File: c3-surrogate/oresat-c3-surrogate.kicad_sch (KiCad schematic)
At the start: 73 parts, among them J1 J-SAMTEC-TFM-120-X1-XXX-D-RA, J2 Conn_01x04, J4 Conn_01x02_Socket, Q1 PMV45EN, Q3 NTR4101P, Q4 NTR4101P, Q5 DMP3050LVT-7, SW2 EG1218, SW3 OS203011MV9QS1, SW4 EG1218, U1 MAX892LEUA+T, U2 LTC4412xS6, U4 LTC4412xS6, U5 TS5A21366, U6 Trinket-M0

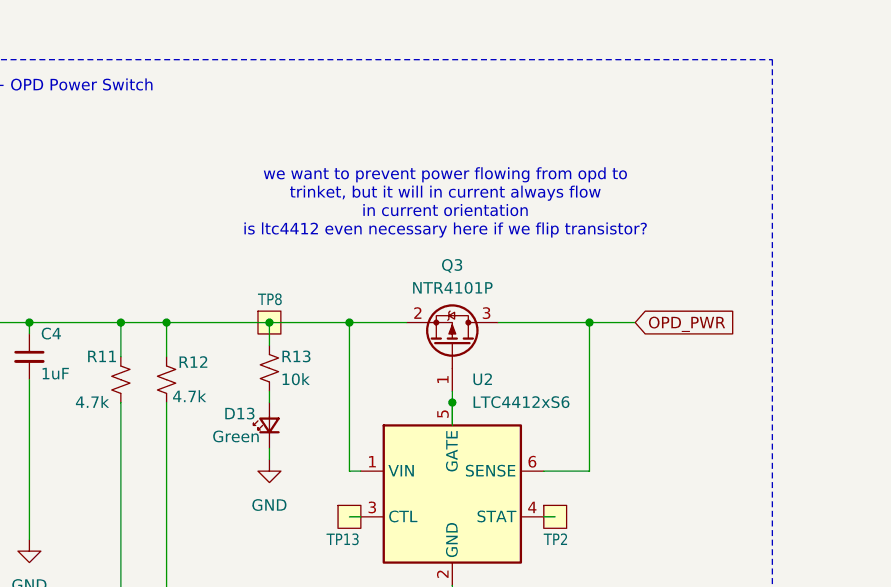
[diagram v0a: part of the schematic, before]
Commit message: fixed transistor that was flipped
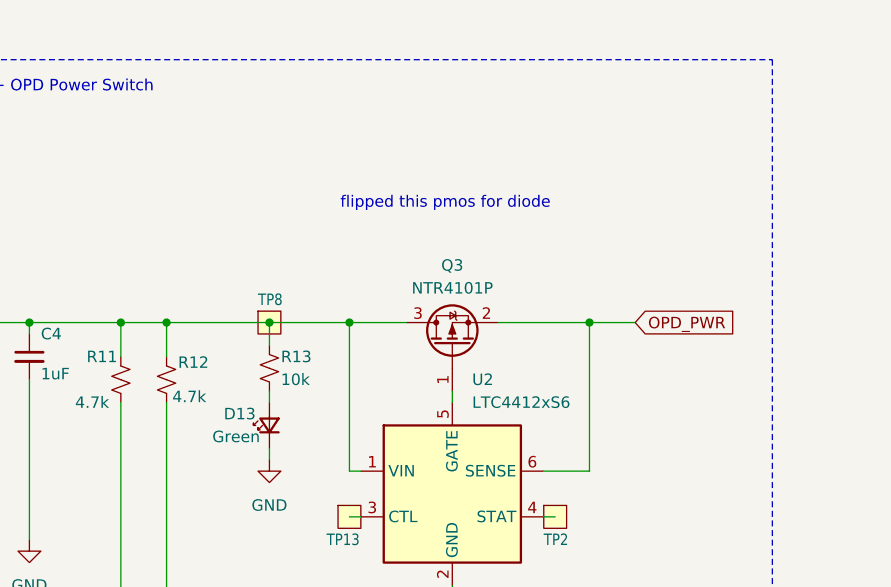
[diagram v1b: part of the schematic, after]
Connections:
- net OPD_PWR: now also Q3.2 (S); no longer Q3.3 (D)
- net at C4.1, R11.1, R12.1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: now also Q3.3 (D); no longer Q3.2 (S)
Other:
- note added: "flipped this pmos for diode"
- note removed: "we want to prevent power flowing from opd to trinket, but it will in current always flow in current orientation is ltc4412 even necessary here if we flip transistor?"
- moved on the sheet: Q3
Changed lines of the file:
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@@
 	)
 	(junction
-		(at 241.3 140.97)
-		(diameter 0)
-		(color 0 0 0 0)
-	)
-	(junction
 		(at 209.55 132.08)
 		(diameter 0.9144)
@@
 	(wire
 		(pts
+			(xy 241.3 139.7) (xy 241.3 140.97)
+		)
+		(stroke
+			(width 0)
+			(type default)
+		)
+	)
+	(wire
+		(pts
 			(xy 220.98 146.05) (xy 220.98 147.32)
 		)
@@
 	(wire
 		(pts
-			(xy 241.3 140.97) (xy 241.3 143.51)
-		)
-		(stroke
-			(width 0)
-			(type default)
-		)
-	)
-	(wire
-		(pts
 			(xy 220.98 132.08) (xy 229.87 132.08)
 		)
@@
 	(wire
 		(pts
-			(xy 241.3 139.7) (xy 241.3 140.97)
-		)
-		(stroke
-			(width 0)
-			(type default)
-		)
-	)
-	(wire
-		(pts
 			(xy 205.74 35.56) (xy 210.82 35.56)
 		)
@@
 		)
 	)
-	(text "we want to prevent power flowing from opd to \ntrinket, but it will in current always flow \nin current orientation\nis ltc4412 even necessary here if we flip transistor?"
+	(text "flipped this pmos for diode"
 		(exclude_from_sim no)
 		(at 240.538 118.872 0)
@@
 	(symbol
 		(lib_id "Transistor_FET:NTR2101P")
-		(at 241.3 134.62 270)
-		(mirror x)
+		(at 241.3 134.62 90)
 		(unit 1)
 		(exclude_from_sim no)
@@
 		)
 		(property "Footprint" "Package_TO_SOT_SMD:SOT-23"
-			(at 239.395 129.54 0)
+			(at 243.205 129.54 0)
 			(effects
 				(font
@@
 		)
 		(property "Datasheet" "http://www.onsemi.com/pub/Collateral/NTR2101P-D.PDF"
-			(at 237.49 129.54 0)
+			(at 245.11 129.54 0)
 			(effects
 				(font

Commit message: fixed another transistor, and minor changes to pcb
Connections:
- net VBUS: now also Q4.2 (S); no longer Q4.3 (D)
- net at Q5.1 (D), Q5.2 (D), Q5.5 (D)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: now also Q4.3 (D); no longer Q4.2 (S)
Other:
- moved on the sheet: Q4
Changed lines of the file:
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@@
 	(symbol
 		(lib_id "Transistor_FET:NTR2101P")
-		(at 200.66 38.1 270)
-		(mirror x)
+		(at 200.66 38.1 90)
 		(unit 1)
 		(exclude_from_sim no)
@@
 		)
 		(property "Footprint" "Package_TO_SOT_SMD:SOT-23"
-			(at 198.755 33.02 0)
+			(at 202.565 33.02 0)
 			(effects
 				(font
@@
 		)
 		(property "Datasheet" "http://www.onsemi.com/pub/Collateral/NTR2101P-D.PDF"
-			(at 196.85 33.02 0)
+			(at 204.47 33.02 0)
 			(effects
 				(font

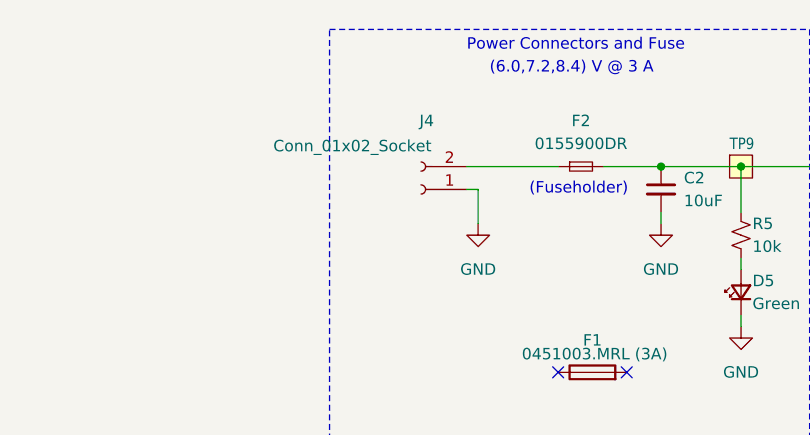
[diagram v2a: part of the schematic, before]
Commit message: edit pcb layout on left side of board (power connectors and sd switch)
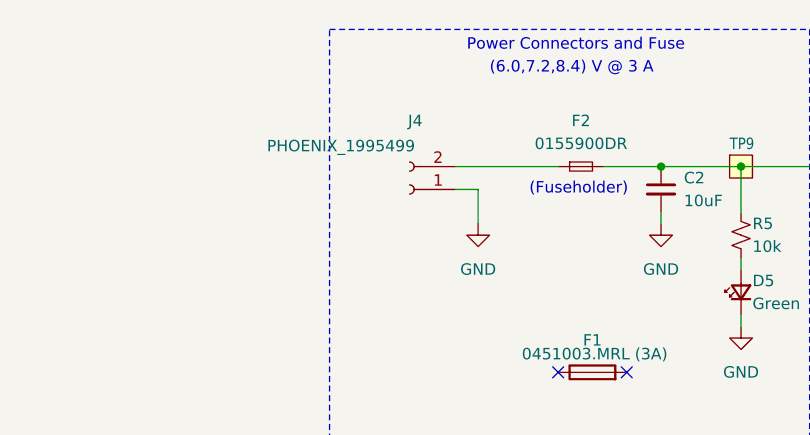
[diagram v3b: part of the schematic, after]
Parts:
- J4: value Conn_01x02_Socket -> PHOENIX_1995499
- SW3: footprint DP3T_OS203011MV9QS1_CNK -> oresat-passives:DP3T_OS203011MV9QS1_CNK
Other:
- moved on the sheet: J4
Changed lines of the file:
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@@
 	(title_block
 		(title "C3 Surrogate Card")
-		(date "2024-07-02")
-		(rev "2")
+		(date "2024-07-09")
+		(rev "\"2\"")
 	)
 	(junction
@@
 	(wire
 		(pts
-			(xy 83.82 35.56) (xy 93.98 35.56)
+			(xy 82.55 35.56) (xy 93.98 35.56)
 		)
 		(stroke
@@
 	(wire
 		(pts
-			(xy 83.82 38.1) (xy 85.09 38.1)
+			(xy 82.55 38.1) (xy 85.09 38.1)
 		)
 		(stroke
@@
 			)
 		)
-		(property "Footprint" "DP3T_OS203011MV9QS1_CNK"
+		(property "Footprint" "oresat-passives:DP3T_OS203011MV9QS1_CNK"
 			(at 327.406 66.548 0)
 			(effects
@@
 	(symbol
 		(lib_id "Connector:Conn_01x02_Socket")
-		(at 78.74 38.1 180)
+		(at 77.47 38.1 180)
 		(unit 1)
 		(exclude_from_sim no)
@@
 		(dnp no)
 		(property "Reference" "J4"
-			(at 79.375 30.48 0)
+			(at 78.105 30.48 0)
 			(effects
 				(font
@@
 			)
 		)
-		(property "Value" "Conn_01x02_Socket"
-			(at 71.12 33.274 0)
+		(property "Value" "PHOENIX_1995499"
+			(at 69.85 33.274 0)
 			(effects
 				(font
@@
 		)
 		(property "Footprint" "oresat-connectors:PHOENIX_1995499"
-			(at 78.74 38.1 0)
+			(at 77.47 38.1 0)
 			(effects
 				(font
@@
 		)
 		(property "Datasheet" "~"
-			(at 78.74 38.1 0)
+			(at 77.47 38.1 0)
 			(effects
 				(font
@@
 		)
 		(property "Description" "Generic connector, single row, 01x02, script generated"
-			(at 78.74 38.1 0)
+			(at 77.47 38.1 0)
 			(effects
 				(font

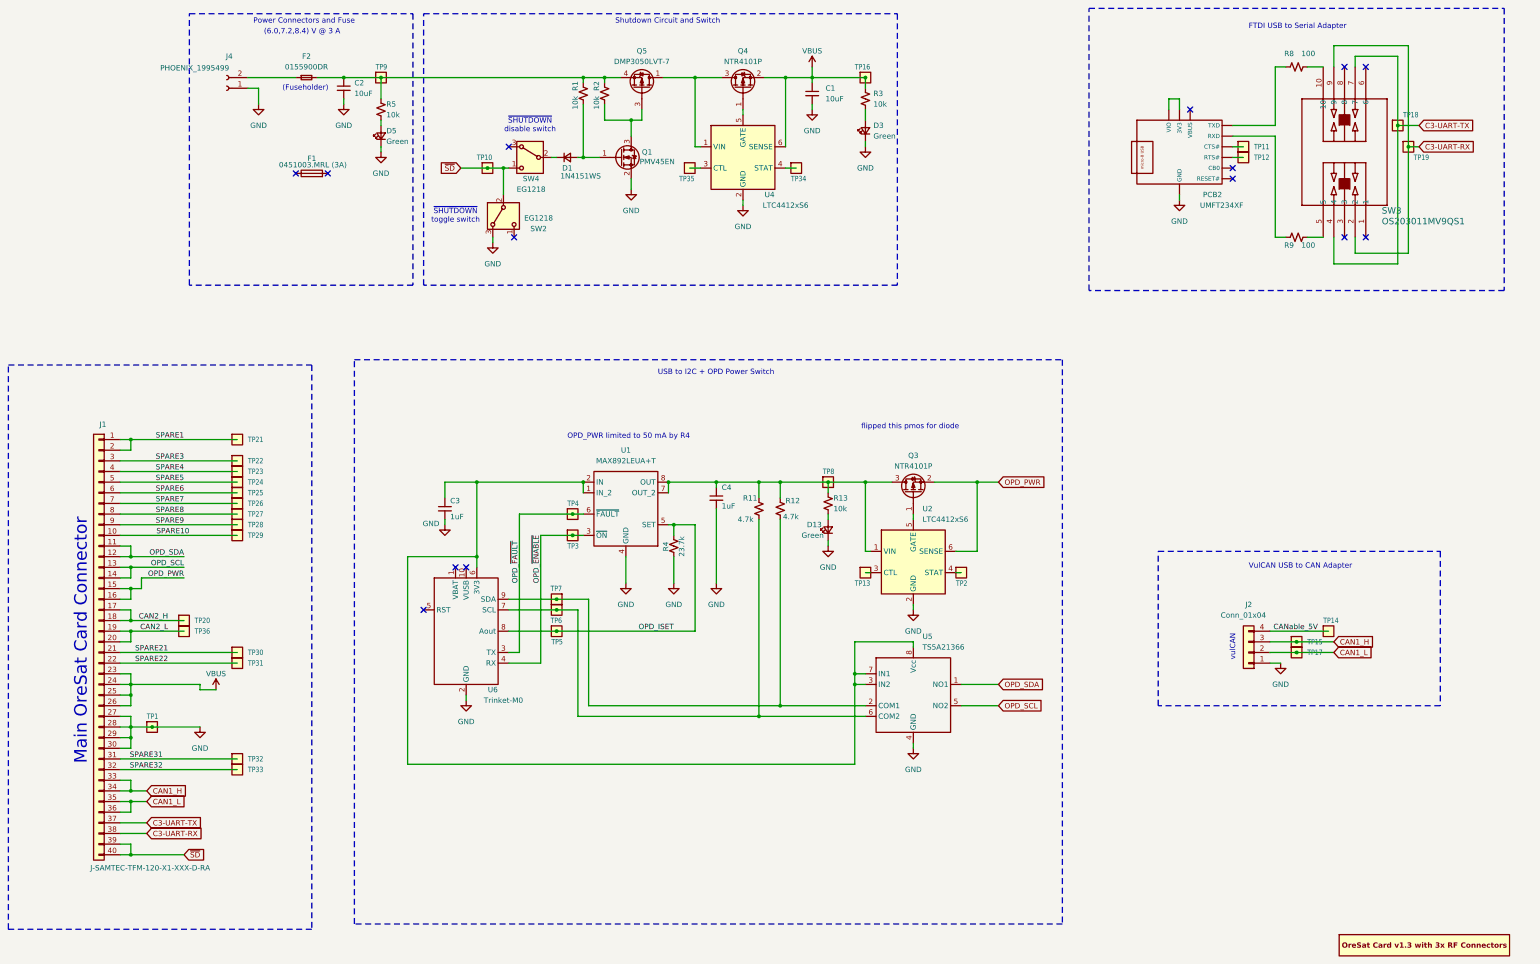
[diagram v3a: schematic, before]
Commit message: Fix schematic, some polish, and began polishing layout.
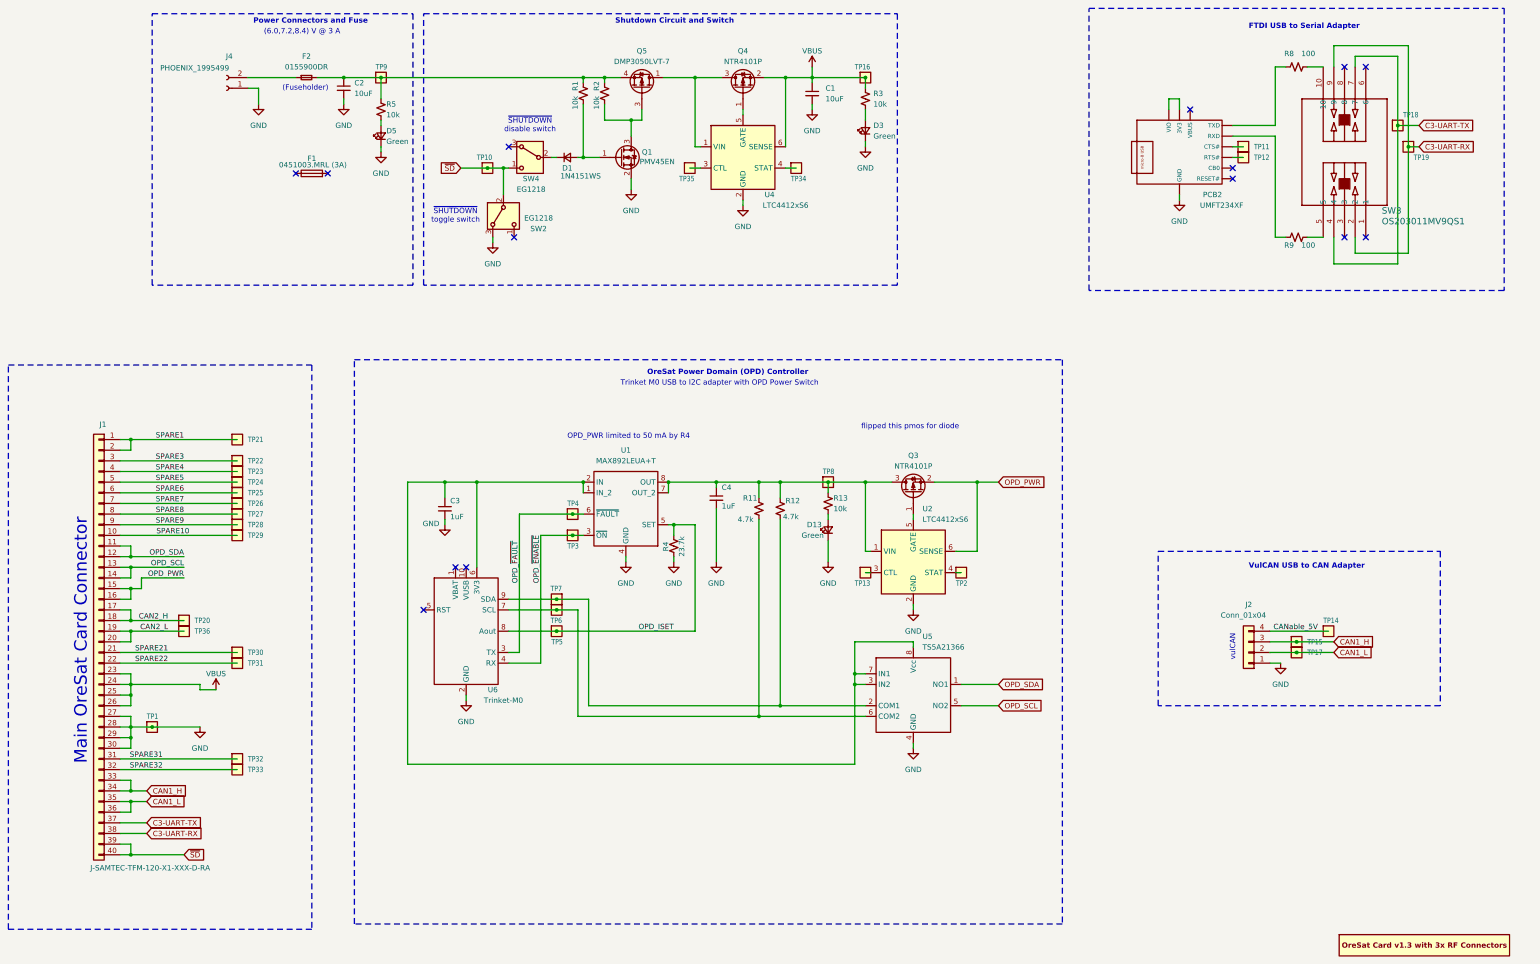
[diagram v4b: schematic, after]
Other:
- note added: "OreSat Power Domain (OPD) Controller"
- note added: "Trinket M0 USB to I2C adapter with OPD Power Switch"
- note removed: "USB to I2C + OPD Power Switch"

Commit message: finished BOM
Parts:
- F1, SW2, SW4: DIST (none) -> Digi-Key; DST Digi-Key -> (none)
- F2: DIST (none) -> Digi-Key; DPN (none) -> 18-01550900DRCT-ND; MFR (none) -> LittelFuse; MPN (none) -> 01550900DR
- J4: DIST (none) -> Digi-Key; DPN (none) -> 277-6718-ND; MFR (none) -> Phoenix Contact; MPN (none) -> 1995499
- PCB2: DIST (none) -> Digi-Key; DPN (none) -> 768-1174-ND; MFR (none) -> FTDI; MPN (none) -> UMFT234XF
- Q3, Q4: DIST (none) -> Digi-Key; DPN (none) -> NTR4101PT1GOSCT-ND; MFR (none) -> Onsemi; MPN (none) -> NTR4101PT1G
- Q5: DIST (none) -> Digi-Key; DPN (none) -> DMP3050LVT-7DICT-ND; MFR (none) -> Diodes Incorporated; MPN (none) -> DMP3050LVT-7
- SW3: DIST (none) -> Digi-Key; DPN (none) -> CKN9557-ND; MFR (none) -> C&K; MPN (none) -> OS203011MV9QS1
- U2, U4: DIST (none) -> Digi-Key; DPN (none) -> 505-LTC4412ES6#TRPBFCT-ND; MFR (none) -> Analog Devices; MPN (none) -> LTC4412ES6#TRPBF
- U5: DIST (none) -> Digi-Key; DPN (none) -> 296-24304-1-ND; MFR (none) -> Texas Instruments; MPN (none) -> TS5A21366DCUR

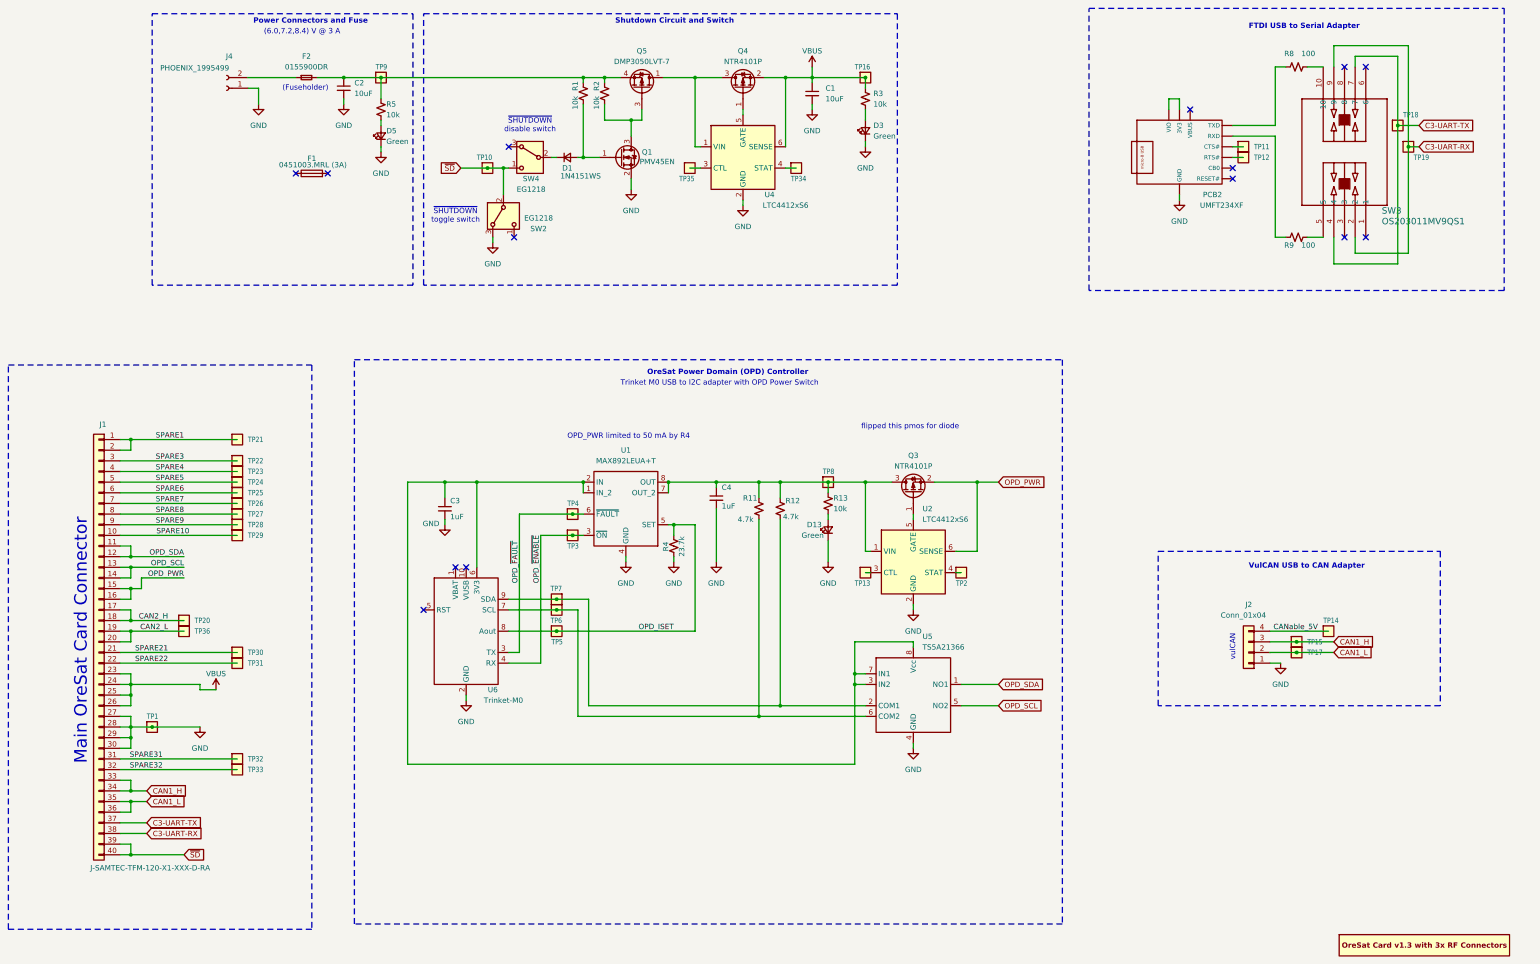
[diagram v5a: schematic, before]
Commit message: Updates for v2 production run, including BOM changes, and polishing of symbols
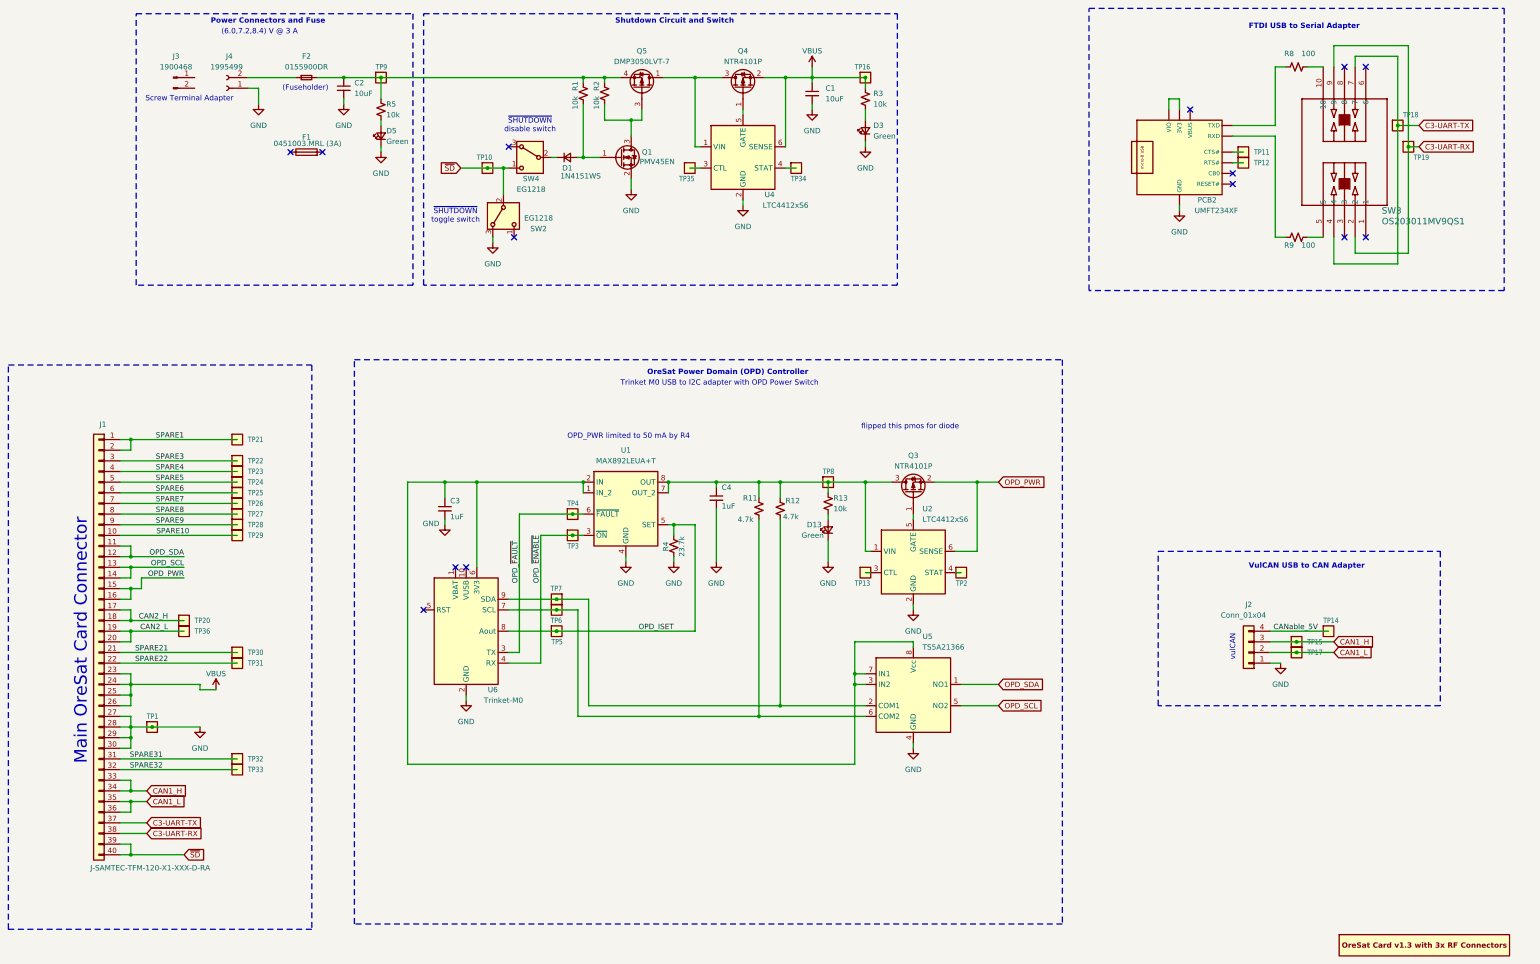
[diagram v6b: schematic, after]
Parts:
- added J3: 1900468, N/A, symbol Connector:Conn_01x02_Pin
- C1, C2: DIST Digi-Key -> DigiKey; DPN 490-10475-1-ND -> 490-12317-1-ND; MFR Murata -> Murata Electronics; MPN GRM188R61A106ME69D -> GRT188R61C106KE13D
- C3, C4: DIST Digi-Key -> DigiKey; DPN 490-GCM188R71E105KA64JCT-ND -> 587-3473-1-ND; MFR Murata -> Taiyo Yuden; MPN GCM188R71E105KA64J -> TMK107BJ105KAHT
- D1, D13, D3, D5, F1, F2, J1, J2, Q1, Q3, Q4, Q5, R11, R12, R4, SW2, SW3, SW4, U2, U4, U5: DIST Digi-Key -> DigiKey
- J4: value PHOENIX_1995499 -> 1995499; DIST Digi-Key -> DigiKey
- PCB1: DIST (none) -> N/A; DPN (none) -> N/A; MFR (none) -> N/A; MPN (none) -> N/A
- PCB2: footprint oresat-misc:UMFT234XF -> oresat-pcbs:UMFT234XF; DIST Digi-Key -> DigiKey
- R1, R13, R2, R3, R5: DIST Digi-Key -> DigiKey; MPN RNCF0603BTE10K0 -> RMCF0603FT10K0
- R8, R9: DIST Digi-Key -> DigiKey; DPN RNCF0603BTE10K0CT-ND -> RMCF0603FT100RCT-ND; MPN RNCF0603BTE10K0 -> RMCF0603FT100R
- TP1, TP10, TP11, TP12, TP13, TP14, TP15, TP16, TP17, TP18, TP19, TP2, TP20, TP21, TP22, TP23, TP24, TP25, TP26, TP27, TP28, TP29, TP3, TP30, TP31, TP32, TP33, TP34, TP35, TP36, TP4, TP5, TP6, TP7, TP8, TP9: DPN (none) -> N/A; MFR (none) -> N/A; MPN (none) -> N/A
- U1: footprint oresat-passives:MAX892 -> U-Maxim-MAX892LEUA+T-power-switch:MAX892LEUA+T
- U6: footprint oresat-mcu:Adafruit-Trinket -> Adafruit-Trinket-M0:Trinket-M0
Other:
- note added: "Screw Terminal Adapter"
- moved on the sheet: F1, TP11, TP12
